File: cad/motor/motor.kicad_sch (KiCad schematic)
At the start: 25 parts, among them Q1 NMOS, Q10 PMOS, Q11 NMOS, Q12 NMOS, Q13 PMOS, Q14 PMOS, Q2 NMOS, Q3 PMOS, Q4 PMOS, Q5 NMOS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

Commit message: more cad
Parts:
- removed PIN_DIR1, PIN_DIR2: 3.3V, symbol Simulation_SPICE:VDC
- removed Q1, Q11, Q12, Q2, Q5, Q9: NMOS, symbol Simulation_SPICE:NMOS
- removed Q10, Q13, Q14, Q3, Q4, Q6, Q7, Q8: PMOS, symbol Simulation_SPICE:PMOS
- removed R10, R2, R5, R9: 100k, symbol Device:R
- removed R4, R6, R7, R8: 10k, symbol Device:R
- added R13, R14: 50, symbol Device:R
- added V2, V3: VPULSE, symbol Simulation_SPICE:VPULSE
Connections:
- net GND: now also V2.2, V3.2
- net VBB: now also V2.1
- net VBB2: now also V3.1
- new net H-Bridge 1/PWR+: R14.1
- new net H-Bridge 1/PWR-: R14.2
- new net H-Bridge 2/PWR+: R13.1
- new net H-Bridge 2/PWR-: R13.2
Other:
- added sheet H-Bridge 1 (hbridge.kicad_sch)
- added sheet H-Bridge 2 (hbridge.kicad_sch)

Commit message: enable/disable
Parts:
- added L1, L2: L, symbol Device:L
- added V4, V5: VPULSE, symbol Simulation_SPICE:VPULSE
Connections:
- net GND: now also V4.2, V5.2
- net H-Bridge 1/PWR+: now also L1.2; no longer R14.1
- net H-Bridge 2/PWR+: now also L2.2; no longer R13.1
- net VBB renamed V_DIR1
- net VBB2 renamed V_DIR2
- new net: L1.1, R14.1
- new net: L2.1, R13.1
- new net V_DISABLE1: V4.1
- new net V_DISABLE2: V5.1
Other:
- sheet H-Bridge 1 ports: added DISABLE; removed none
- sheet H-Bridge 2 ports: added DISABLE; removed none
- moved on the sheet: R13, R14, V1, V2, V3

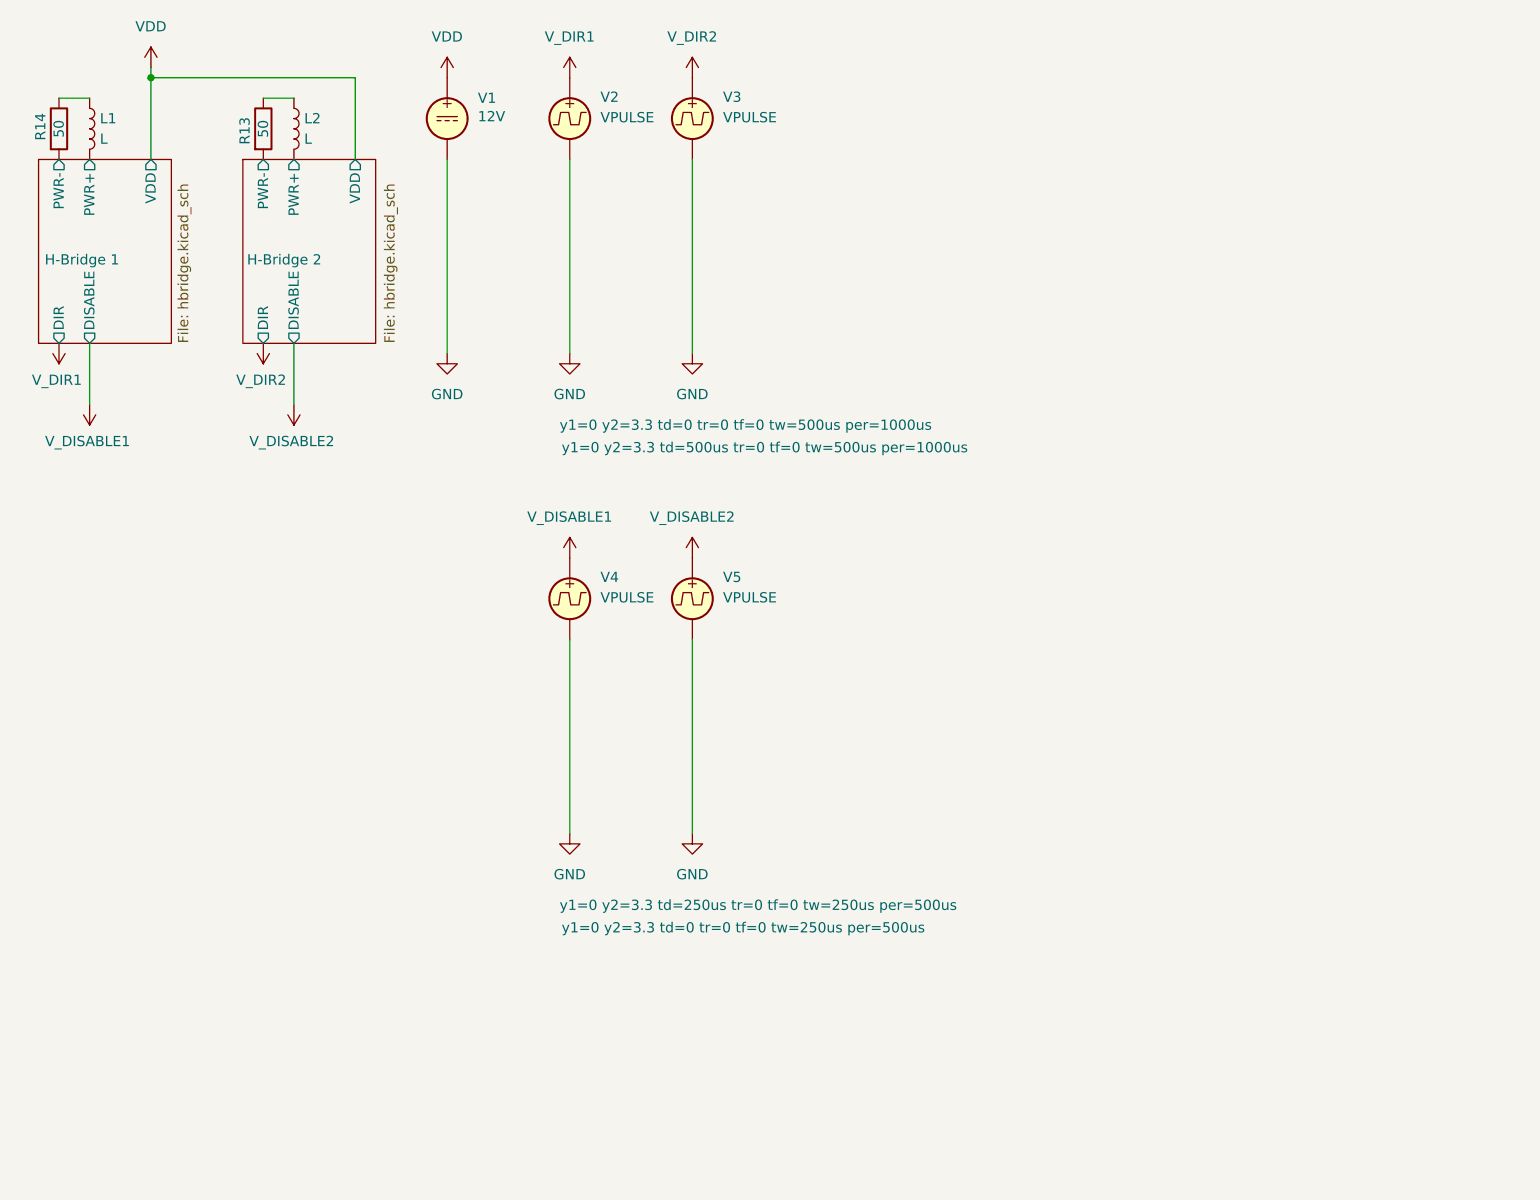
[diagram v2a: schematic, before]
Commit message: reliable enable/disable with capacitor
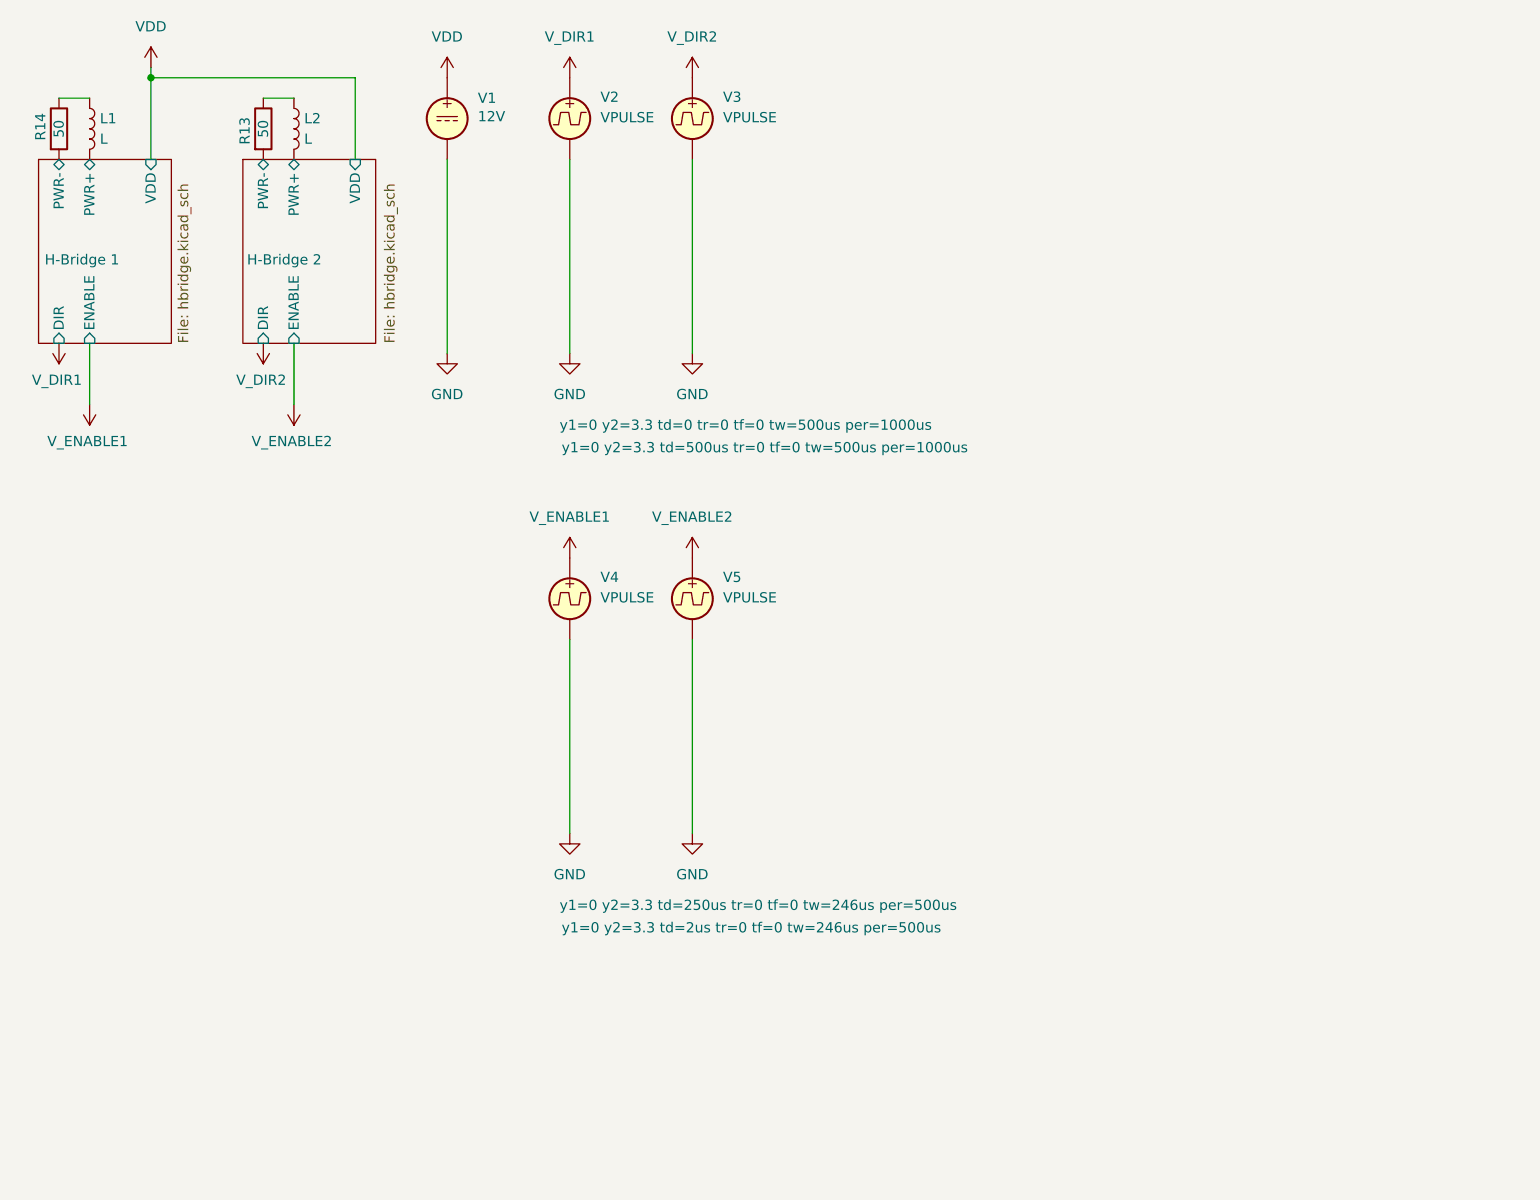
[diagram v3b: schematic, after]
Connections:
- net V_DISABLE1 renamed V_ENABLE1
- net V_DISABLE2 renamed V_ENABLE2
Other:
- sheet H-Bridge 1 ports: added ENABLE; removed DISABLE
- sheet H-Bridge 2 ports: added ENABLE; removed DISABLE
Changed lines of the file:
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@@
 			)
 		)
-		(property "Sim.Params" "y1=0 y2=3.3 td=0 tr=0 tf=0 tw=250us per=500us"
+		(property "Sim.Params" "y1=0 y2=3.3 td=2us tr=0 tf=0 tw=246us per=500us"
 			(at 87.884 128.524 0)
 			(effects
@@
 			)
 		)
-		(property "Value" "V_DISABLE1"
+		(property "Value" "V_ENABLE1"
 			(at 28.956 68.072 0)
 			(effects
@@
 			)
 		)
-		(property "Sim.Params" "y1=0 y2=3.3 td=250us tr=0 tf=0 tw=250us per=500us"
+		(property "Sim.Params" "y1=0 y2=3.3 td=250us tr=0 tf=0 tw=246us per=500us"
 			(at 87.63 125.73 0)
 			(effects
@@
 			)
 		)
-		(property "Value" "V_DISABLE2"
+		(property "Value" "V_ENABLE2"
 			(at 104.14 77.47 0)
 			(effects
@@
 			)
 		)
-		(property "Value" "V_DISABLE2"
+		(property "Value" "V_ENABLE2"
 			(at 54.356 68.072 0)
 			(effects
@@
 			)
 		)
-		(property "Value" "V_DISABLE1"
+		(property "Value" "V_ENABLE1"
 			(at 88.9 77.47 0)
 			(effects
@@
 			)
 		)
-		(pin "VDD" output
+		(pin "VDD" input
 			(at 62.23 33.02 90)
 			(effects
@@
 			)
 		)
-		(pin "DIR" output
+		(pin "DIR" input
 			(at 50.8 55.88 270)
 			(effects
@@
 			)
 		)
-		(pin "PWR+" output
+		(pin "PWR+" bidirectional
 			(at 54.61 33.02 90)
 			(effects
@@
 			)
 		)
-		(pin "PWR-" output
+		(pin "PWR-" bidirectional
 			(at 50.8 33.02 90)
 			(effects
@@
 			)
 		)
-		(pin "DISABLE" output
+		(pin "ENABLE" input
 			(at 54.61 55.88 270)
 			(effects
@@
 			)
 		)
-		(pin "VDD" output
+		(pin "VDD" input
 			(at 36.83 33.02 90)
 			(effects
@@
 			)
 		)
-		(pin "DIR" output
+		(pin "DIR" input
 			(at 25.4 55.88 270)
 			(effects
@@
 			)
 		)
-		(pin "PWR+" output
+		(pin "PWR+" bidirectional
 			(at 29.21 33.02 90)
 			(effects
@@
 			)
 		)
-		(pin "PWR-" output
+		(pin "PWR-" bidirectional
 			(at 25.4 33.02 90)
 			(effects
@@
 			)
 		)
-		(pin "DISABLE" output
+		(pin "ENABLE" input
 			(at 29.21 55.88 270)
 			(effects

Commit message: solve amp spikes
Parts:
- renumbered R14 to R1, R13 to R2, V4 to V3, V3 to V4
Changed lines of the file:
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@@
 		(on_board yes)
 		(dnp no)
-		(property "Reference" "V4"
+		(property "Reference" "V3"
 			(at 92.71 84.9601 0)
 			(effects
@@
 			)
 		)
-		(property "Sim.Params" "y1=0 y2=3.3 td=2us tr=0 tf=0 tw=246us per=500us"
+		(property "Sim.Params" "y1=0 y2=3.3 td=0us tr=0us tf=0us tw=250us per=500us"
 			(at 87.884 128.524 0)
 			(effects
@@
 			(project "motor"
 				(path "/833cc0fc-e321-4f55-9543-54c4634b471c"
-					(reference "V4")
+					(reference "V3")
 					(unit 1)
 				)
@@
 		(on_board yes)
 		(dnp no)
-		(property "Reference" "#PWR026"
+		(property "Reference" "#PWR02"
 			(at 29.21 59.69 0)
 			(effects
@@
 			(project "motor"
 				(path "/833cc0fc-e321-4f55-9543-54c4634b471c"
-					(reference "#PWR026")
+					(reference "#PWR02")
 					(unit 1)
 				)
@@
 			)
 		)
-		(property "Sim.Params" "y1=0 y2=3.3 td=250us tr=0 tf=0 tw=246us per=500us"
+		(property "Sim.Params" "y1=0 y2=3.3 td=250us tr=0us tf=0us tw=250us per=500us"
 			(at 87.63 125.73 0)
 			(effects
@@
 		(dnp no)
 		(fields_autoplaced yes)
-		(property "Reference" "#PWR013"
+		(property "Reference" "#PWR06"
 			(at 73.66 26.67 0)
 			(effects
@@
 			(project "motor"
 				(path "/833cc0fc-e321-4f55-9543-54c4634b471c"
-					(reference "#PWR013")
+					(reference "#PWR06")
 					(unit 1)
 				)
@@
 		(dnp no)
 		(fields_autoplaced yes)
-		(property "Reference" "#PWR02"
+		(property "Reference" "#PWR07"
 			(at 73.66 63.5 0)
 			(effects
@@
 			(project "motor"
 				(path "/833cc0fc-e321-4f55-9543-54c4634b471c"
-					(reference "#PWR02")
+					(reference "#PWR07")
 					(unit 1)
 				)
@@
 		(dnp no)
 		(fields_autoplaced yes)
-		(property "Reference" "#PWR015"
+		(property "Reference" "#PWR09"
 			(at 88.9 63.5 0)
 			(effects
@@
 			(project "motor"
 				(path "/833cc0fc-e321-4f55-9543-54c4634b471c"
-					(reference "#PWR015")
+					(reference "#PWR09")
 					(unit 1)
 				)
@@
 		(on_board yes)
 		(dnp no)
-		(property "Reference" "V3"
+		(property "Reference" "V4"
 			(at 107.95 25.2701 0)
 			(effects
@@
 			(project "motor"
 				(path "/833cc0fc-e321-4f55-9543-54c4634b471c"
-					(reference "V3")
+					(reference "V4")
 					(unit 1)
 				)
@@
 		(on_board yes)
 		(dnp no)
-		(property "Reference" "#PWR030"
+		(property "Reference" "#PWR01"
 			(at 25.4 52.07 0)
 			(effects
@@
 			(project "motor"
 				(path "/833cc0fc-e321-4f55-9543-54c4634b471c"
-					(reference "#PWR030")
+					(reference "#PWR01")
 					(unit 1)
 				)
@@
 		(on_board yes)
 		(dnp no)
-		(property "Reference" "R14"
+		(property "Reference" "R1"
 			(at 23.114 28.956 90)
 			(effects
@@
 			(project "motor"
 				(path "/833cc0fc-e321-4f55-9543-54c4634b471c"
-					(reference "R14")
+					(reference "R1")
 					(unit 1)
 				)
@@
 		(dnp no)
 		(fields_autoplaced yes)
-		(property "Reference" "#PWR07"
+		(property "Reference" "#PWR08"
 			(at 88.9 26.67 0)
 			(effects
@@
 			(project "motor"
 				(path "/833cc0fc-e321-4f55-9543-54c4634b471c"
-					(reference "#PWR07")
+					(reference "#PWR08")
 					(unit 1)
 				)
@@
 		(dnp no)
 		(fields_autoplaced yes)
-		(property "Reference" "#PWR019"
+		(property "Reference" "#PWR014"
 			(at 104.14 86.36 0)
 			(effects
@@
 			(project "motor"
 				(path "/833cc0fc-e321-4f55-9543-54c4634b471c"
-					(reference "#PWR019")
+					(reference "#PWR014")
 					(unit 1)
 				)
@@
 		(dnp no)
 		(fields_autoplaced yes)
-		(property "Reference" "#PWR021"
+		(property "Reference" "#PWR015"
 			(at 104.14 123.19 0)
 			(effects
@@
 			(project "motor"
 				(path "/833cc0fc-e321-4f55-9543-54c4634b471c"
-					(reference "#PWR021")
+					(reference "#PWR015")
 					(unit 1)
 				)
@@
 		(dnp no)
 		(fields_autoplaced yes)
-		(property "Reference" "#PWR024"
+		(property "Reference" "#PWR013"
 			(at 104.14 63.5 0)
 			(effects
@@
 			(project "motor"
 				(path "/833cc0fc-e321-4f55-9543-54c4634b471c"
-					(reference "#PWR024")
+					(reference "#PWR013")
 					(unit 1)
 				)
@@
 		(dnp no)
 		(fields_autoplaced yes)
-		(property "Reference" "#PWR017"
+		(property "Reference" "#PWR011"
 			(at 88.9 123.19 0)
 			(effects
@@
 			(project "motor"
 				(path "/833cc0fc-e321-4f55-9543-54c4634b471c"
-					(reference "#PWR017")
+					(reference "#PWR011")
 					(unit 1)
 				)
@@
 		(on_board yes)
 		(dnp no)
-		(property "Reference" "R13"
+		(property "Reference" "R2"
 			(at 48.514 29.464 90)
 			(effects
@@
 			(project ""
 				(path "/833cc0fc-e321-4f55-9543-54c4634b471c"
-					(reference "R13")
+					(reference "R2")
 					(unit 1)
 				)
@@
 		(on_board yes)
 		(dnp no)
-		(property "Reference" "#PWR027"
+		(property "Reference" "#PWR05"
 			(at 54.61 59.69 0)
 			(effects
@@
 			(project "motor"
 				(path "/833cc0fc-e321-4f55-9543-54c4634b471c"
-					(reference "#PWR027")
+					(reference "#PWR05")
 					(unit 1)
 				)
@@
 		(dnp no)
 		(fields_autoplaced yes)
-		(property "Reference" "#PWR029"
+		(property "Reference" "#PWR03"
 			(at 36.83 25.4 0)
 			(effects
@@
 			(project "motor"
 				(path "/833cc0fc-e321-4f55-9543-54c4634b471c"
-					(reference "#PWR029")
+					(reference "#PWR03")
 					(unit 1)
 				)
@@
 		(dnp no)
 		(fields_autoplaced yes)
-		(property "Reference" "#PWR023"
+		(property "Reference" "#PWR012"
 			(at 104.14 26.67 0)
 			(effects
@@
 			(project "motor"
 				(path "/833cc0fc-e321-4f55-9543-54c4634b471c"
-					(reference "#PWR023")
+					(reference "#PWR012")
 					(unit 1)
 				)
@@
 		(dnp no)
 		(fields_autoplaced yes)
-		(property "Reference" "#PWR016"
+		(property "Reference" "#PWR010"
 			(at 88.9 86.36 0)
 			(effects
@@
 			(project "motor"
 				(path "/833cc0fc-e321-4f55-9543-54c4634b471c"
-					(reference "#PWR016")
+					(reference "#PWR010")
 					(unit 1)
 				)
@@
 		(on_board yes)
 		(dnp no)
-		(property "Reference" "#PWR012"
+		(property "Reference" "#PWR04"
 			(at 50.8 52.07 0)
 			(effects
@@
 			(project "motor"
 				(path "/833cc0fc-e321-4f55-9543-54c4634b471c"
-					(reference "#PWR012")
-					(unit 1)
-				)
+					(reference "#PWR04")
+					(unit 1)
+				)

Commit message: more stuff
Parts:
- removed V1: 12V, symbol Simulation_SPICE:VDC
- added V1: VPULSE, symbol Simulation_SPICE:VPULSE
- L1, L2: value L -> 15mH
- renumbered V4 to V2, V2 to V3, V3 to V4
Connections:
- net GND: now also V1.2
- net VDD: now also V1.1
- net V_DIR1 renamed V1_GATE2
- net V_DIR2 renamed V1_GATE1
- net V_ENABLE1 renamed V2_GATE1
- net V_ENABLE2 renamed V2_GATE2
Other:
- added sheet galvo_driver (galvo.kicad_sch)
- sheet H-Bridge 1 ports: added G1, G2, GND; removed DIR, ENABLE
- sheet H-Bridge 2 ports: added G1, G2, GND; removed DIR, ENABLE
- moved on the sheet: V2, V3, V4, V5
